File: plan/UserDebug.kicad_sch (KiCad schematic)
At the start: 0 parts

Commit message: Create UserDebug schematic
- Status LED
- Pair Button
- Pogo Pin Adapter Pad (for programming)
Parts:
- added D1: APT1608LZGCK, LED_SMD:LED_0603_1608Metric, symbol Device:LED
- added J1: Debug_SWD_Pogo_2x3, Smarthome:Debug_SWD_Pogo_2x3_P2.00mm, symbol Smarthome:Debug_SWD_Pogo_2x3
- added R1: 2.2 kΩ, 1%, Resistor_SMD:R_0402_1005Metric, symbol Device:R
- added SW1: EVPBB2A9B000, Smarthome:Button_Panasonic_EVPBB_2.6x1.6mm, symbol Smarthome:Button_Panasonic_EVPBB2A9B000
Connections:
- new net: D1.2 (A), R1.2
- new net GND: D1.1 (K), J1.2 (GND), SW1.1
- new net PA01: J1.4 (SWCLK)
- new net PA02: J1.3 (SWDIO)
- new net PA03: J1.6 (SWO)
- new net PC08: R1.1
- new net PC09: SW1.2
- new net VBAT: J1.1 (VTARGET)
- new net ~{RESET}: J1.5 (~{RESET})

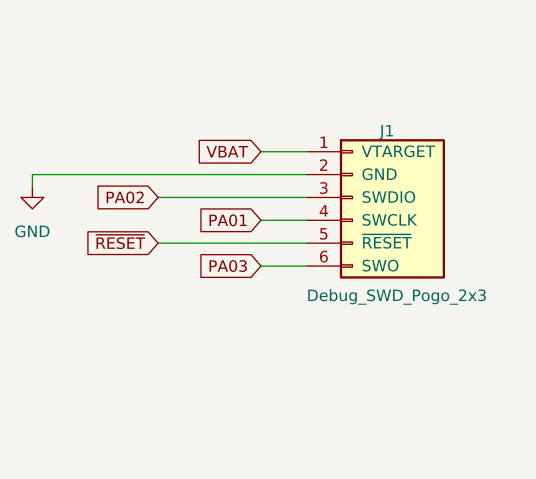
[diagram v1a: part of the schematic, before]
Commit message: Adapt schematics to pass ERC
- Clean AVDD / IOVDD / VREGVDD: use VBAT instead
- Clean DVDD / VDCDC: remove net DVDD and use VDCDC instead
- Use original symbol from library for J1
- Mark VBAT / VDCDC / RFVDD / PAVDD / GND with PWR_FLAG
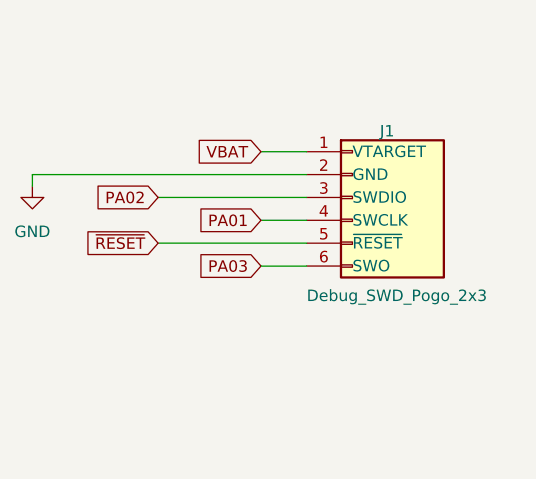
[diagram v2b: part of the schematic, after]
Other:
- moved on the sheet: J1

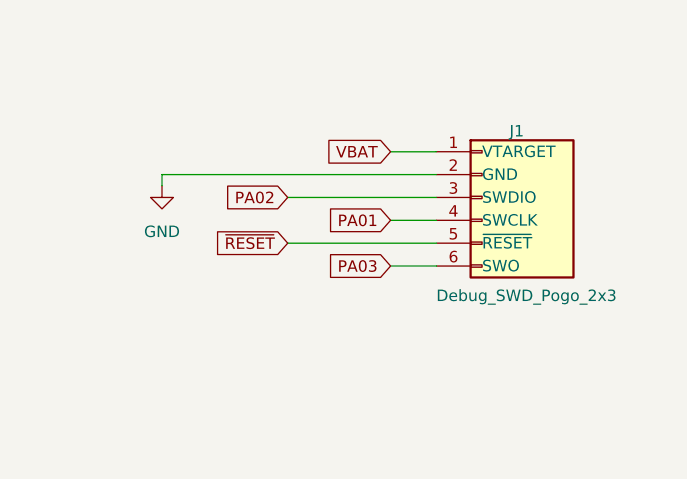
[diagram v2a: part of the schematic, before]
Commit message: Adapt and place programming/debug pad
- Remove NPTH holes because they require too much space
- Place pad on board bottom side
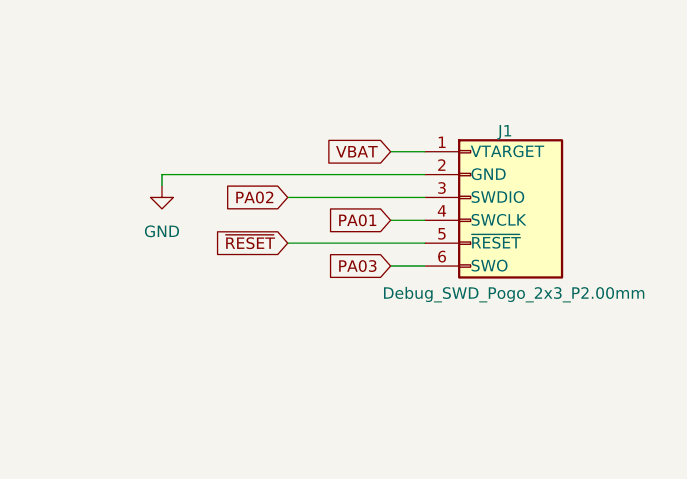
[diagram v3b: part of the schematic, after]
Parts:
- J1: value Debug_SWD_Pogo_2x3 -> Debug_SWD_Pogo_2x3_P2.00mm
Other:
- moved on the sheet: J1
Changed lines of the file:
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@@
 	(wire
 		(pts
-			(xy 193.04 80.01) (xy 223.52 80.01)
+			(xy 193.04 80.01) (xy 222.25 80.01)
 		)
 		(stroke
@@
 	(wire
 		(pts
-			(xy 207.01 82.55) (xy 223.52 82.55)
-		)
-		(stroke
-			(width 0)
-			(type default)
-		)
-	)
-	(wire
-		(pts
-			(xy 207.01 87.63) (xy 223.52 87.63)
-		)
-		(stroke
-			(width 0)
-			(type default)
-		)
-	)
-	(wire
-		(pts
-			(xy 193.04 81.28) (xy 193.04 80.01)
-		)
-		(stroke
-			(width 0)
-			(type default)
-		)
-	)
-	(wire
-		(pts
-			(xy 218.44 77.47) (xy 223.52 77.47)
+			(xy 207.01 82.55) (xy 222.25 82.55)
+		)
+		(stroke
+			(width 0)
+			(type default)
+		)
+	)
+	(wire
+		(pts
+			(xy 207.01 87.63) (xy 222.25 87.63)
+		)
+		(stroke
+			(width 0)
+			(type default)
+		)
+	)
+	(wire
+		(pts
+			(xy 193.04 80.01) (xy 193.04 81.28)
+		)
+		(stroke
+			(width 0)
+			(type default)
+		)
+	)
+	(wire
+		(pts
+			(xy 218.44 77.47) (xy 222.25 77.47)
 		)
 		(stroke
@@
 	(wire
 		(pts
-			(xy 218.44 85.09) (xy 223.52 85.09)
-		)
-		(stroke
-			(width 0)
-			(type default)
-		)
-	)
-	(wire
-		(pts
-			(xy 218.44 90.17) (xy 223.52 90.17)
+			(xy 218.44 85.09) (xy 222.25 85.09)
+		)
+		(stroke
+			(width 0)
+			(type default)
+		)
+	)
+	(wire
+		(pts
+			(xy 218.44 90.17) (xy 222.25 90.17)
 		)
 		(stroke
@@
 	(symbol
 		(lib_id "Smarthome:Debug_SWD_Pogo_2x3")
-		(at 228.6 82.55 0)
+		(at 227.33 82.55 0)
 		(unit 1)
 		(body_style 1)
@@
 		(dnp no)
 		(property "Reference" "J1"
-			(at 231.648 75.184 0)
+			(at 230.378 75.184 0)
 			(show_name no)
 			(do_not_autoplace no)
@@
 			)
 		)
-		(property "Value" "Debug_SWD_Pogo_2x3"
-			(at 223.52 93.472 0)
-			(show_name no)
-			(do_not_autoplace no)
-			(effects
-				(font
-					(size 1.27 1.27)
-				)
-				(justify left)
+		(property "Value" "Debug_SWD_Pogo_2x3_P2.00mm"
+			(at 232.156 93.218 0)
+			(show_name no)
+			(do_not_autoplace no)
+			(effects
+				(font
+					(size 1.27 1.27)
+				)
 			)
 		)
 		(property "Footprint" "Smarthome:Debug_SWD_Pogo_2x3_P2.00mm"
-			(at 228.6 82.55 0)
+			(at 227.33 82.55 0)
 			(hide yes)
 			(show_name no)
@@
 		)
 		(property "Datasheet" ""
-			(at 228.6 82.55 0)
-			(hide yes)
-			(show_name no)
-			(do_not_autoplace no)
-			(effects
-				(font
-					(size 1.27 1.27)
-				)
-			)
-		)
-		(property "Description" "6-pin SWD programming interface with 2x3 pogo pads and two asymmetric NPTH alignment holes"
-			(at 228.6 82.55 0)
-			(hide yes)
-			(show_name no)
+			(at 227.33 82.55 0)
+			(hide yes)
+			(show_name no)
+			(do_not_autoplace no)
+			(effects
+				(font
+					(size 1.27 1.27)
+				)
+			)
+		)
+		(property "Description" "6-pin SWD pogo programming interface, 2x3, 2.00 mm pitch, without alignment holes"
+			(at 227.33 82.55 0)
+			(hide yes)
+			(show_name no)
